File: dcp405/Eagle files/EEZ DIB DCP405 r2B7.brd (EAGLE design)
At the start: 180 x 95 mm, 311 parts, among them IC1 LTC3864EMSE#PBF, IC10 MC33272ADR2G, IC11 LTC2050HVCS8#PBF, IC12 74AUP1G74DC.125, IC13 MCP23S17-E/SS, IC14 REF5025AIDR, IC15 TC77-5.0MCTTR, IC16 DAC8552IDGKR, IC17 SN74LVC1G3157DCKR, IC18 ADS1120IPWR, IC19 LM293D, IC2 TPS54060DGQ, IC20 MAX9141ESA, IC3 SI8641BB-B-IS1, IC4 SN74LVC1G139DCUR, IC5 MC78L05, IC6 MC79L05, IC7 SI8641BB-B-IS1, IC8 M24C32-WMN6P, IC9 MC33272ADR2G, J1 4907, J2 FCR7350R, J3 FCR7350B, K1 G6K-2F-5DC, Q1 SUD19P06-60, Q10 PSMN0R9-25YLC, Q11 PSMN0R9-25YLC, Q12 BSS84P, Q13 BTA26-600, Q14 FMMT493TA, Q15 2N7002, Q16 2N7002, Q17 2N7002, Q18 MMBT5401, Q19 MMBT5551, Q2 MMBT5401, Q20 MMBT5551, Q21 2N7002, Q3 D45H11FP, Q4 D45H11FP, Q5 FQPF11P06 or FQPF27P06, Q6 BCP56-16.115, Q7 MMBT5401, Q8 NZT605, Q9 BSS205NH6327XTSA1, X1 39-30-1020, X2 77317-104-28LF, X3 1844249, X4 DS1024-2*10R0

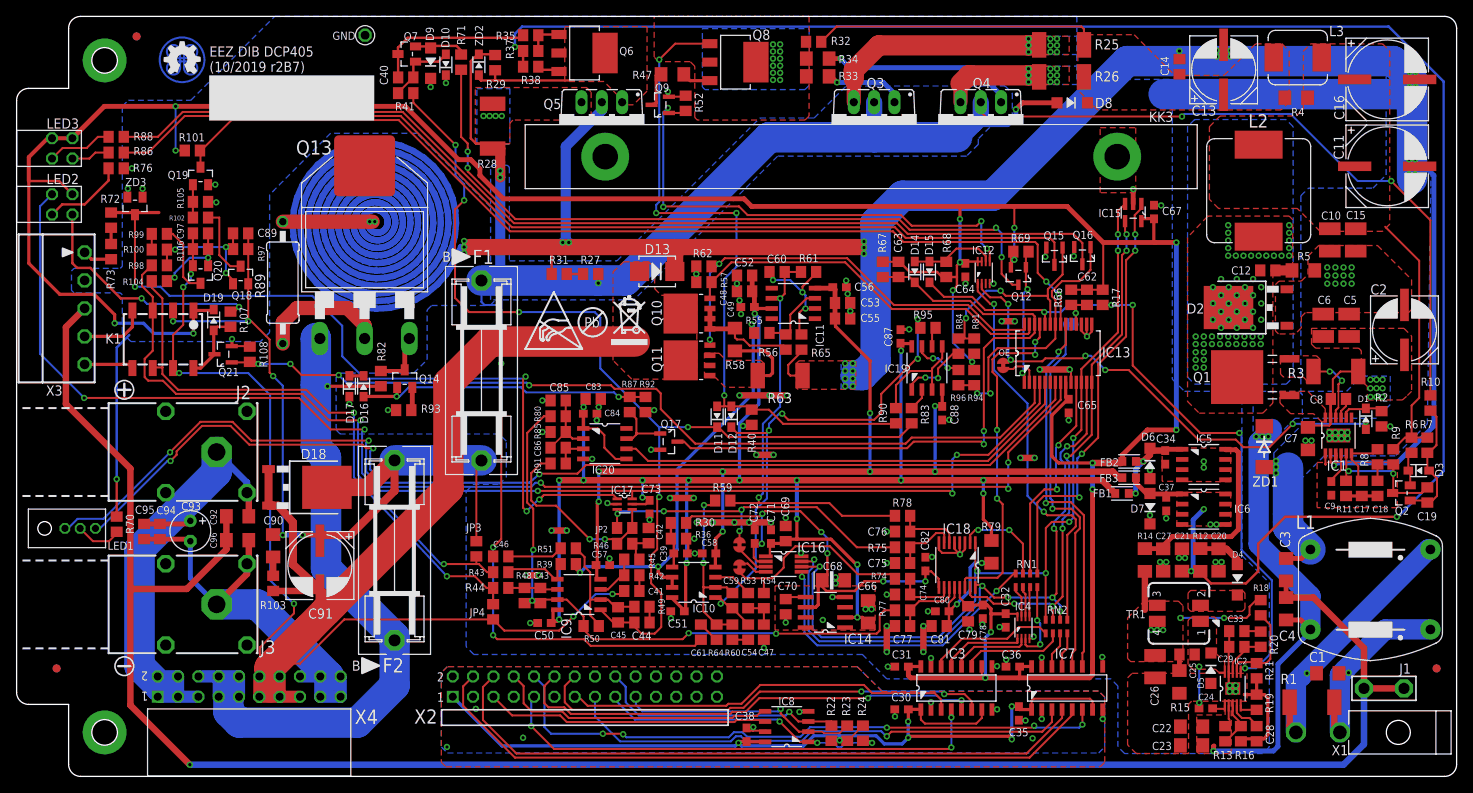
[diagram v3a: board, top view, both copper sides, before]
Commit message: DCP405 Q18 added to HW OVP
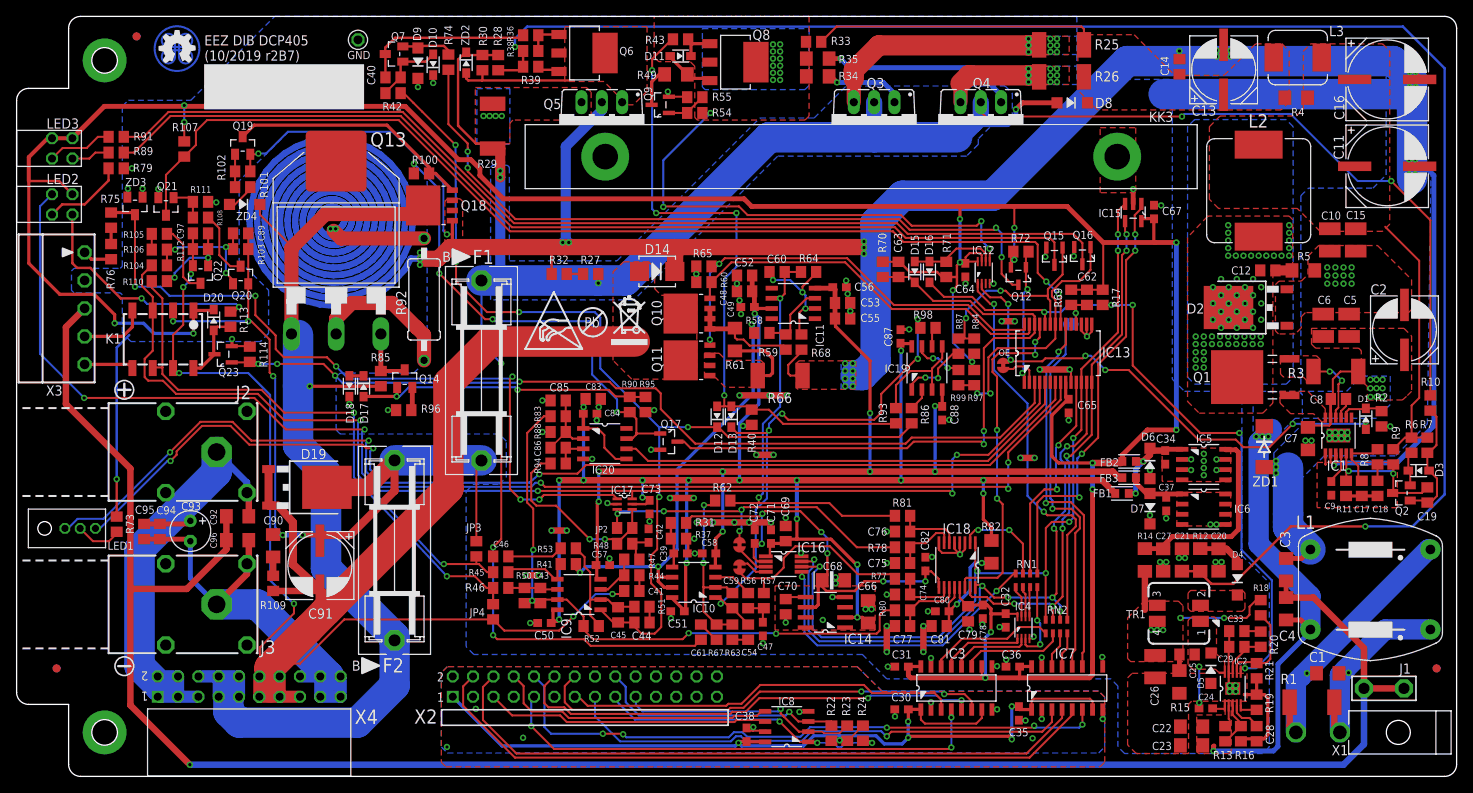
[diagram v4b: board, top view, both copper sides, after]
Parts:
- added D20: BAS316, EEZ_Lib1:SOD323-R
- added Q22: MMBT5551, transistor:SOT23-BEC
- added Q23: 2N7002, EEZ_Lib1:SOT103P240X110-3N
- added R109: 1R, rcl:R0805
- added R110: 750R, rcl:R0805
- added R111: 47K, rcl:R0805
- added R112: 330R, rcl:R0805
- added R113: 470R, rcl:R0805
- added R114: 100K, rcl:R0805
- added ZD4: MMSZ5230BT1G, EEZ_Lib1:SOD123
- C40: value 470p -> N.C.
- C41, C46: value 220p -> 100p
- C42, C47: value 470n -> 100n; device rcl:C0805 -> rcl:C0603
- C43, C60: value 33p -> N.C.
- C44: value 330p -> N.C.
- D13: value SK55 -> BAS316; device EEZ_Lib1:SMB -> EEZ_Lib1:SOD323-R
- D14: value BAS316 -> SK55; device EEZ_Lib1:SOD323-R -> EEZ_Lib1:SMB
- D18: value SK10100D1-DIO -> BAS316; device EEZ_Lib1:TO252-L -> EEZ_Lib1:SOD323-R
- D19: value BAS316 -> SK10100D1-DIO; device EEZ_Lib1:SOD323-R -> EEZ_Lib1:TO252-L
- IC9: value MC33272ADR2G -> TL072D
- Q18: value MMBT5401 -> PSMN013-60YL; device transistor:SOT23-BEC -> EEZ_Lib1:SOT669
- Q20: value MMBT5551 -> MMBT5401
- Q21: value 2N7002 -> MMBT5551; device EEZ_Lib1:SOT103P240X110-3N -> transistor:SOT23-BEC
- R100: value 2K2 -> 1K
- R101, R102: value 10K -> 22K
- R103: value 1R -> 330R
- R105: value 47K -> 1K
- R106, R80: value 330R -> 2K2
- R107: value 470R -> 10K
- R108, R52: value 100K -> 10K
- R28: value 2R2/2W -> 100K; device rcl:R2512 -> rcl:R0805
- R29: value 4K7 -> 2R2/2W; device rcl:R0805 -> rcl:R2512
- R30: value 10K -> 4K7
- R31, R67, R94: value 4K7 -> 10K
- R32: value 2K2 -> 4K7
- R33: value 10R -> 2K2; device rcl:R1206 -> rcl:R0805
- R35: value 5K6 -> 10R; device rcl:R0805 -> rcl:R1206
- R36: value 220R -> 4K7
- R37: value 1K -> 220R
- R38: value 220R -> 1K
- R39: value 7K5 0.1% -> 220R
- R41: value 22K -> 7K5 0.1%
- R42: value 4K7 -> 22K
- R43: value 124K 0.1% -> 1K
- R44: value 124K 0.1% -> 10K
- R45: value 10K -> 124K 0.1%
- R46: value 2K2 -> 124K 0.1%
- R47: value 15R -> 10K; device rcl:R1206 -> rcl:R0805
- R48: value 7K5 0.1% -> 2K2
- R49: value 2K2 -> 15R; device rcl:R0805 -> rcl:R1206
- R50: value 10K -> 7K5 0.1%
- R51: value 4K7 -> N.C.
- R53, R71: value 2K2 -> 10K
- R54: value 2K2 -> 220R
- R55: value 39K 0.1% -> 100K
- R56: value 820R 0.1% -> 2K2
- R57: value 47K -> 2K2
- R58: value 1R -> 39K 0.1%; device rcl:R1206 -> rcl:R0805
- R59, R68: value 10K -> 820R 0.1%
- R60: value 1K -> 47K
- R61: value 39K 0.1% -> 1R; device rcl:R0805 -> rcl:R1206
- R62: value 47K -> 10K
- R63: value 0R010 (low TCR) -> 1K; device EEZ_Lib1:R_2512-4WIRE -> rcl:R0805
- R64: value 10K -> 39K 0.1%
- R65: value 820R 0.1% -> 47K
- R66: value 1K -> 0R010 (low TCR); device rcl:R0805 -> EEZ_Lib1:R_2512-4WIRE
- R69: value 100K -> 1K
- R70: value 270R -> 4K7
- R72: value 470R -> 100K
- R73: value 470R -> 270R
- R75: value 2K2 -> 470R
- R79: value 10R -> 470R; device rcl:R1206 -> rcl:R0805
- R81: value 4K7 -> 2K2
- R82: value 470R -> 10R; device rcl:R0805 -> rcl:R1206
- R83, R91: value 10K -> 330R
- R85: value 10K -> 470R
- R86, R88: value 330R -> 10K
- R87, R99: value 1K -> 4K7
- R89: value AC01000001007JA100 -> 330R; device rcl:0411/15 -> rcl:R0805
- R90: value 10K -> 1K
- R92: value 100K -> AC01000001007JA100; device rcl:R0805 -> rcl:0411/15
- R93: value 6R2 -> 10K
- R95: value 10K -> 100K
- R96: value 4K7 -> 6R2
- R97: value 330R -> 4K7
- R98: value 750R -> 10K
- moved R79 119.5 mm to (12.4, 76.0), turned to 180 degrees
- moved R72 113.8 mm to (125.5, 65.6), turned to 0 degrees
- moved R75 107.1 mm to (11.8, 69.5), turned to 270 degrees
- moved R86 104.7 mm to (111.9, 45.1), turned to 90 degrees
- moved R99 101.5 mm to (117.7, 49.8), turned to 270 degrees
- moved R70 100.9 mm to (108.3, 63.4), turned to 270 degrees
- moved R98 96.4 mm to (113.9, 56.1)
- moved R97 93.1 mm to (119.7, 49.8), turned to 90 degrees
- moved R74 86.0 mm to (54.0, 89.3), turned to 270 degrees
- moved R82 79.3 mm to (121.9, 28.1)
- moved D16 72.2 mm to (114.1, 63.1), turned to 90 degrees
- moved R43 70.3 mm to (83.0, 92.1), turned to 0 degrees
- moved R96 69.5 mm to (48.4, 45.8), turned to 0 degrees
- moved R91 68.7 mm to (12.4, 79.9), turned to 180 degrees
- moved R42 67.2 mm to (47.1, 85.4)
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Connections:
- new net -9V: C21.1, R12.1, R28.1, R38.2, R39.2
- new net N$24: R101.2, ZD4.A
- new net N$28: Q19.B, R101.1, R102.2
- new net N$44: Q18.4, Q19.C, R100.1
- new net N$46: D11.C, Q8.1, R43.2
- new net N$53: Q9.1, R54.1, R55.2
- net !DP_DRIVE: now also R74.1; no longer R71.1
- net !IOEXP_RST: now also R69.2; no longer R66.2
- net !OVP_FAULT: now also D15.C, R70.2; no longer D14.C, R67.2
- net !SET_DP: now also R72.2; no longer R69.2
- net +5V: now also D20.C, R107.2, R70.1, R71.1, R72.1, R84.2, R97.2; no longer D19.C, R101.2, R66.1, R67.1, R68.1, R81.2, R94.2
- net +VREF: now also R31.1; no longer R30.1
- net -12V: no longer C21.1, R12.1, R37.2, R38.2
- net 50MA_S: now also R59.1, R61.1; no longer R56.1, R58.1
- net 5A_S: now also R66.2; no longer R63.2
- net AUX_IN: now also R75.1; no longer R72.1
- net CC_ACTIVE: now also R97.1, R99.2; no longer R94.1, R96.2
- net CC_LED: now also R91.2; no longer R88.2
- net CURR_50MA: now also R60.2; no longer R57.2
- net CURR_5A: now also R65.2; no longer R62.2
- net CV_ACTIVE: now also R84.1, R87.2; no longer R81.1, R84.2
- net CV_LED: now also R89.1; no longer R86.1
- net DARL_C: now also R35.1; no longer R32.1
- net DP_S: now also R29.1; no longer R28.1
- net D_CC: now also R91.1; no longer R88.1
- net D_CV: now also R89.2; no longer R86.2
- net GCOM: now also R41.1, R58.1; no longer R39.1, R55.1
- net GND: now also D18.C, Q21.E, Q23.2, R111.1, R114.1, R37.2, R55.1, R60.1, R65.1, R73.2, R79.1, R88.2, R95.1, R96.1; no longer D17.C, Q19.E, Q21.2, R105.1, R108.1, R36.2, R52.1, R57.1, R62.1, R70.2, R76.1, R85.2, R92.1, R93.1
- net ISENSE+: now also R58.2, R59.2; no longer R55.2, R56.2
- net ISENSE-: now also R64.1, R68.2; no longer R61.1, R65.2
- net I_MON: now also R62.1, R64.2, R81.1; no longer R59.1, R61.2, R78.1
- net I_SERVO: now also D13.C, R98.1; no longer D12.C, R95.1
- net I_SET: now also R57.1, R77.1; no longer R54.1, R74.1
- net LOOP_CTRL: now also D13.A, R43.1, R93.2; no longer D11.A, Q8.1, R90.2
- net N$10: now also R56.1, R57.2; no longer R53.1, R54.2
- net N$102: now also R31.2, R37.1; no longer R30.2, R36.1
- net N$105: now also R87.1; no longer R84.1
- net N$106: now also R99.1; no longer R96.1
- net N$107: now also Q20.B, R103.1, R104.2, R106.2; no longer Q18.B, R100.2, R97.1, R98.2
- net N$108: now also Q20.C, R108.2; no longer Q18.C, R102.2
- net N$109: now also Q22.C, R105.1; no longer Q20.C, R99.1
- net N$11: now also R61.2, R66.2S; no longer R58.2, R63.2S
- net N$110: now also Q22.B, R110.1, R112.2; no longer Q20.B, R104.1, R106.2
- net N$112: now also Q21.B, R108.1, R111.2; no longer Q19.B, R102.1, R105.2
- net N$113: now also R109.2; no longer R103.2
- net N$114: now also D20.A, Q23.3, R113.1; no longer D19.A, Q21.3, R107.1
- net N$12: now also R73.1; no longer R70.1
- net N$120: now also R113.2; no longer R107.2
- net N$121: now also R79.2; no longer R76.2
- net N$13: now also R100.2, R90.2; no longer R87.2
- net N$14: now also R51.2; no longer R49.2
- net N$15: now also R92.2; no longer R89.2
- net N$150: now also R41.2, R45.1; no longer R39.2, R43.1
- net N$153: now also R86.2; no longer R83.2
- net N$158: now also R46.1, R50.2; no longer R44.1, R48.2
- net N$161: now also R98.2; no longer R95.2
- net N$17: now also R75.2, R76.1; no longer R72.2, R73.1
- net N$170: now also R93.1; no longer R90.1
- net N$173: now also R105.2, R106.1; no longer R100.1, R99.2
- net N$18: now also R85.1; no longer R82.1
- net N$19: now also R96.2; no longer R93.2
- net N$20: now also D17.C, D18.A; no longer D16.C, D17.A
- net N$200: now also R66.1S, R68.1; no longer R63.1S, R65.1
- net N$21: now also D17.A, R90.1, R95.2; no longer D16.A, R87.1, R92.2
- net N$31: now also R94.2; no longer R91.2
- net N$32: now also R76.2; no longer R73.2
- net N$33: now also R83.2, R88.1; no longer R80.2, R85.1
- net N$35: now also R49.1; no longer R47.1
- net N$37: now also R63.1; no longer R60.1
- net N$39: now also R36.1, R38.1; no longer R35.1, R37.1
- net N$40: now also R35.2; no longer R34.2
- net N$42: now also R74.2; no longer R71.2
- net N$43: now also R34.2; no longer R33.2
- net N$45: now also R36.2; no longer R35.2
- net N$47: now also D11.A, R49.2; no longer R47.2
- net N$49: now also R32.2; no longer R31.2
- net N$55: now also R42.2; no longer R41.2
- net N$56: now also D16.A, R71.2; no longer D14.A, R68.2
- net N$70: now also R82.2; no longer R79.2
- net N$72: now also R77.2; no longer R74.2
- net N$73: now also R80.2; no longer R77.2
- net N$80: now also R78.2; no longer R75.2
- net N$81: now also R81.2; no longer R78.2
- net N$82: now also R56.2; no longer R53.2
- net N$83: now also R44.2, R47.2; no longer R42.2, R45.2
- net N$84: now also R51.1, R52.2, R53.2; no longer R49.1, R50.2, R51.2
- net N$88: now also R67.1; no longer R64.1
- net N$89: now also R62.2, R63.2, R67.2; no longer R59.2, R60.2, R64.2
- net N$90: now also R44.1; no longer R42.1
- net N$91: now also R53.1; no longer R51.1
- net N$98: now also R39.1; no longer R38.1
- net OUTF+: now also Q18.MB, R85.2, ZD4.C; no longer R82.2
- net POST_OE: now also R54.2; no longer Q9.1, R52.2
- net POST_OUT+: now also R29.2, R30.1; no longer R29.1
- net POST_OUT-: now also D14.A, D19.1, D19.2, Q22.E, R109.1, R112.1; no longer D13.A, D18.1, D18.2, Q20.E, R103.1, R106.1
- net POST_OUTF+: now also D19.3, Q20.E, R103.2; no longer D18.3, Q18.E, R97.2
- net PREG_OUT+: now also R33.2; no longer R32.2
- net PREG_OUT-: now also D14.C, Q18.1, Q18.2, Q18.3, Q19.E, R102.1, R32.1, R66.1, R92.1; no longer D13.C, R31.1, R63.1, R89.1
- net PWRGOOD: now also D16.C; no longer D15.C
- net Q6C: now also R30.2; no longer R29.2
- net RSENSE: now also Q23.1, R114.2; no longer Q21.1, R108.2
- net SENSE+: now also R104.1, R45.2; no longer R43.2, R98.1
- net SENSE-: now also R110.2, R46.2; no longer R104.2, R44.2
- net SENSE_ERR: now also Q21.C, R107.1; no longer Q19.C, R101.1
- net U_MON: now also R52.1, R83.1; no longer R48.1, R77.1
- net U_SERVO: now also D12.C, R42.1, R86.1; no longer D11.C, R41.1, R83.1
- net U_SET: now also R78.1; no longer R75.1
- net U_SET_OUT: now also R48.1, R94.1; no longer R46.1, R91.1
- net U_SET_OVP: now also R47.1, R48.2; no longer R45.1, R46.2
- net V+: now also R82.1; no longer R79.1
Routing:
- net -12V: track 222.5 -> 0.00 mm, vias 4 -> 0
- net -9V: track 0.00 -> 218.0 mm, vias 0 -> 2
- net N$13: track 8.24 -> 59.5 mm, vias 0 -> 4
- net PREG_OUT-: track 587.5 -> 631.7 mm, vias 23 -> 25
- net OUTF+: track 94.6 -> 134.0 mm
- net N$44: track 0.00 -> 30.6 mm
- net SENSE_ERR: track 125.9 -> 135.4 mm
- net AUX_IN: track 101.4 -> 96.1 mm, vias 4 -> 6
- net N$46: track 0.00 -> 5.17 mm
- net N$53: track 0.00 -> 5.04 mm
- net N$28: track 0.00 -> 4.11 mm
- net N$24: track 0.00 -> 3.64 mm
- net LOOP_CTRL: track 84.6 -> 81.2 mm
- net N$47: track 3.58 -> 6.45 mm
- net N$15: track 16.2 -> 18.5 mm
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
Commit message: DCP405 OE slow down
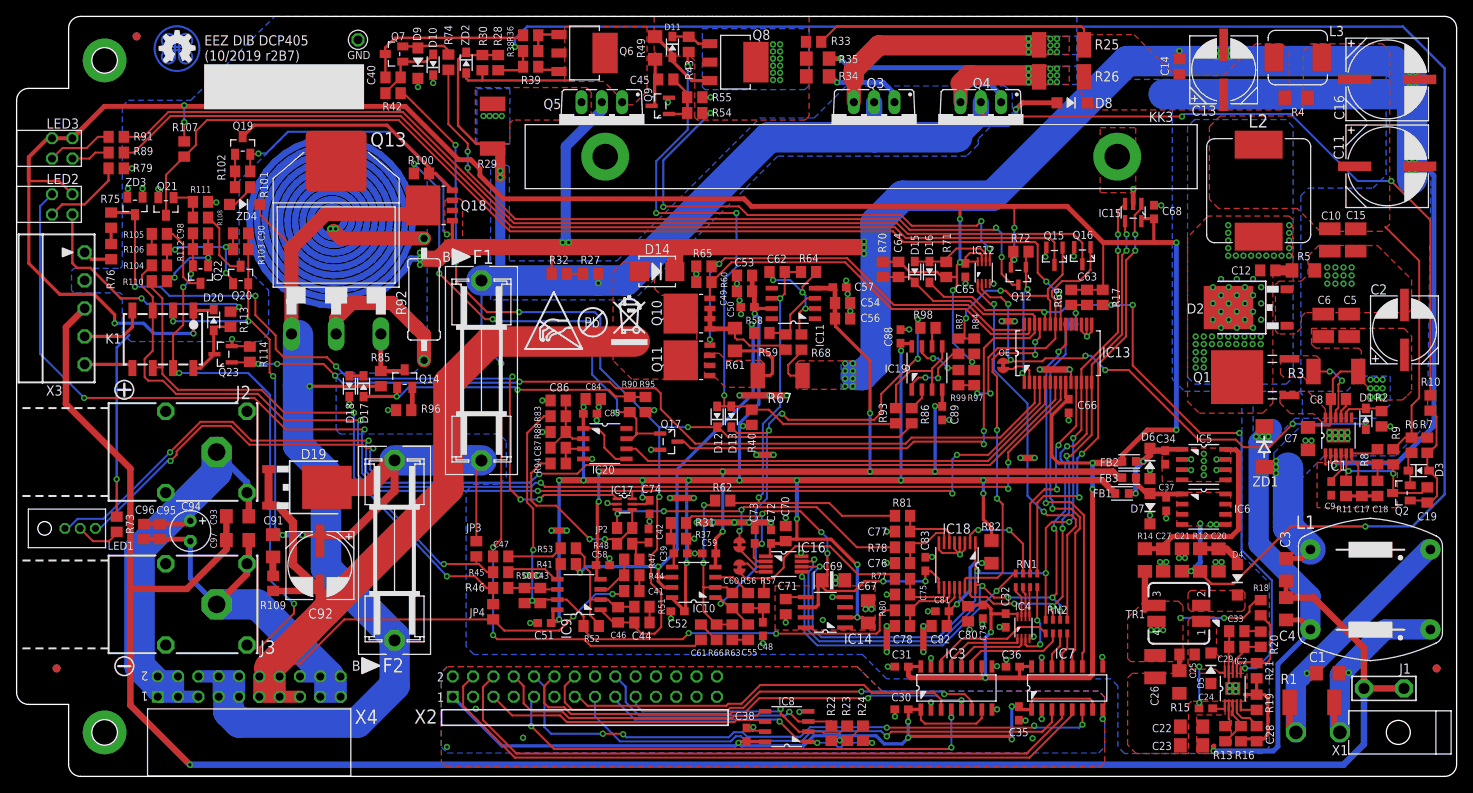
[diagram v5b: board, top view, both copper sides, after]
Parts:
- added C98: 10n, rcl:C0805
- C45: value 33p -> 1u
- C46: value 100p -> 33p
- C47: value 100n -> 100p; device rcl:C0603 -> rcl:C0805
- C48, C89: value 10n -> 100n; device rcl:C0805 -> rcl:C0603
- C49: value 100n -> 10n; device rcl:C0603 -> rcl:C0805
- C52, C79, C81: value 1u -> 100n; device rcl:C0805 -> rcl:C0603
- C53: value 10n -> 1u
- C54: value 6n8 -> 10n
- C55: value 1u -> 6n8
- C56, C71, C80, C82: value 100n -> 1u; device rcl:C0603 -> rcl:C0805
- C59: value 33p -> 100n; device rcl:C0805 -> rcl:C0603
- C60: value N.C. -> 33p
- C62: value 330p -> N.C.
- C63: value 1n -> 330p
- C64: value 100n -> 1n; device rcl:C0603 -> rcl:C0805
- C66: value 4u7 -> 100n; device rcl:C1206 -> rcl:C0603
- C67: value 100n -> 4u7; device rcl:C0603 -> rcl:C1206
- C68: value 4u7 tant. -> 100n; device EEZ_Lib1:EC1206 -> rcl:C0603
- C69: value 1u -> 4u7 tant.; device rcl:C0805 -> EEZ_Lib1:EC1206
- C74: value 4n7 -> 100n; device rcl:C0805 -> rcl:C0603
- C78: value 100n -> 4n7; device rcl:C0603 -> rcl:C0805
- C83: value N.C. -> 100n; device rcl:C0805 -> rcl:C0603
- C84: value 100n -> N.C.; device rcl:C0603 -> rcl:C0805
- C85: value 1n -> 100n; device rcl:C0805 -> rcl:C0603
- C86: value 33n -> 1n
- C87: value 100n -> 33n; device rcl:C0603 -> rcl:C0805
- C90: value 470n -> 10n; device rcl:C1206 -> rcl:C0805
- C91: value HHXC630A330MHA0G -> 470n; device EEZ_Lib1:CAPAE830X1050N -> rcl:C1206
- C92: value 10n/200V -> HHXC630A330MHA0G; device rcl:C1206 -> EEZ_Lib1:CAPAE830X1050N
- C93: value N.C. -> 10n/200V; device EEZ_Lib1:ECAP2/5 -> rcl:C1206
- C94: device rcl:C0805 -> EEZ_Lib1:ECAP2/5
- C96: value 10n/200V -> N.C.; device rcl:C1206 -> rcl:C0805
- C97: value 10n -> 10n/200V; device rcl:C0805 -> rcl:C1206
- KK1, KK2: value PCB-MB-01 -> PMB-1
- R44, R53: value 10K -> 16K
- R54: value 220R -> 4K7
- R55: value 100K -> N.C.
- R66: value 0R010 (low TCR) -> 10K; device EEZ_Lib1:R_2512-4WIRE -> rcl:R0805
- R67: value 10K -> 0R010 (low TCR); device rcl:R0805 -> EEZ_Lib1:R_2512-4WIRE
- moved C89 90.5 mm to (115.7, 45.4), turned to 90 degrees
- moved C45 67.2 mm to (81.2, 87.1), turned to 180 degrees
- moved C67 61.4 mm to (106.4, 20.6)
- moved C68 61.0 mm to (142.2, 70.5), turned to 90 degrees
- moved C50 47.0 mm to (91.4, 58.7), turned to 180 degrees
- moved C83 46.4 mm to (113.6, 26.5), turned to 270 degrees
- moved C57 45.6 mm to (102.9, 61.2), turned to 0 degrees
- moved C87 45.0 mm to (67.7, 41.1), turned to 0 degrees
- moved C54 42.8 mm to (103.3, 59.2), turned to 180 degrees
- moved C52 42.8 mm to (82.6, 20.6)
- moved C48 42.3 mm to (93.3, 18.4), turned to 270 degrees
- moved C60 41.5 mm to (89.5, 22.0), turned to 270 degrees
- moved C55 40.9 mm to (91.4, 18.0), turned to 90 degrees
- moved C90 39.3 mm to (28.0, 67.9), turned to 180 degrees
- moved C62 38.9 mm to (95.1, 63.1), turned to 0 degrees
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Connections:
- removed net -12V: IC6.2, IC6.3, IC6.6, IC6.7
- net !IOEXP_RST: now also C63.1; no longer C62.1
- net !OVP_FAULT: now also C64.1; no longer C63.1
- net +5V: now also C65.2, C66.1, C68.1, C80.2; no longer C62.2, C65.1, C67.1, C78.2
- net +VREF: now also C69.+, C73.2, C83.2; no longer C68.+, C72.2, C82.2
- net -9V: now also IC6.2, IC6.3, IC6.6, IC6.7
- net 5A_S: now also R67.2; no longer R66.2
- net GND: now also C48.2, C49.1, C50.2, C54.1, C56.1, C57.2, C59.1, C65.1, C68.2, C69.-, C71.2, C73.1, C74.2, C76.1, C77.2, C83.1, C84.2, C86.1, C89.1; no longer C47.2, C48.1, C49.2, C50.1, C55.1, C56.2, C57.1, C64.1, C65.2, C68.-, C69.2, C71.1, C73.2, C74.1, C76.2, C77.1, C83.2, C84.1, C87.1
- net ISENSE-: now also C62.1; no longer C60.1
- net I_MON: now also C62.2; no longer C60.2
- net I_SERVO: now also C55.2, C60.2; no longer C54.2, C59.2
- net N$10: now also C48.1; no longer C47.1
- net N$107: now also C90.2; no longer C89.2
- net N$11: now also R67.2S; no longer R66.2S
- net N$110: now also C98.1; no longer C97.1
- net N$113: now also C91.2; no longer C90.2
- net N$200: now also R67.1S; no longer R66.1S
- net N$31: now also C87.2; no longer C86.2
- net N$33: now also C86.2, C87.1; no longer C85.2, C86.1
- net N$35: now also C45.2
- net N$37: now also C55.1; no longer C54.1
- net N$53: now also C45.1
- net N$70: now also C82.2; no longer C80.2
- net N$71: now also C71.1; no longer C70.1
- net N$72: now also C75.2; no longer C74.2
- net N$73: now also C78.2; no longer C77.2
- net N$80: now also C76.2; no longer C75.2
- net N$81: now also C77.1; no longer C76.1
- net N$84: now also C46.1; no longer C45.1
- net N$88: now also R66.1; no longer R67.1
- net N$89: now also C60.1, R66.2; no longer C59.1, R67.2
- net N$91: now also C47.2; no longer C46.2
- net OUTC+: now also C93.1, C94.+, C96.1; no longer C92.1, C93.+, C94.1
- net OUTC-: now also C94.-, C97.2; no longer C93.-, C94.2
- net PE: now also C93.2, C97.1; no longer C92.2, C96.1
- net POST_OUT+: now also C47.1; no longer C46.1
- net POST_OUT-: now also C92.-, C98.2; no longer C91.-, C97.2
- net POST_OUTF+: now also C91.1, C92.+; no longer C89.1, C91.+
- net PREG_OUT-: now also R67.1; no longer R66.1
- net U_SERVO: now also C46.2; no longer C45.2
- net V+: now also C49.2, C50.1, C53.2, C67.1, C70.1, C72.2, C74.1, C84.1, C85.2, C88.2; no longer C48.2, C49.1, C50.2, C66.1, C69.1, C71.2, C73.1, C83.1, C84.2, C87.2
- net V-: now also C54.2, C56.2, C57.1, C59.2, C89.2; no longer C53.2, C55.2, C56.1, C57.2, C88.2
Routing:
- net -9V: track 218.0 -> 224.5 mm, vias 2 -> 4
- net N$47: track 6.45 -> 9.67 mm
- net N$53: track 5.04 -> 7.24 mm
- net N$35: track 4.88 -> 6.54 mm
- net LOOP_CTRL: track 81.2 -> 80.0 mm
- net OUTF+: track 134.0 -> 134.8 mm
- net GND: track 202.5 -> 202.2 mm, vias 121 -> 122
- added copper zone on layer 1, net -9V
- removed copper zone on layer 1, net -12V
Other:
- board text added: "0R"
- board text added: "Parts with red marked values are installed on DCP405 only Solder JP2, JP3, JP4 (0R 0805) and use wire jumper instead of F1 and F2 on DCP405B"

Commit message: DCP405 Eagle files updated
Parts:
- R28: value 100K -> N.C.
- X3: value 1844249 -> 691322110005
- moved C45 0.45 mm to (80.7, 87.2)
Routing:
- net LOOP_CTRL: track 80.0 -> 82.2 mm
- net POST_OE: track 61.7 -> 63.1 mm
- net -9V: track 224.5 -> 223.9 mm
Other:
- board text added: "EEZ DIB DCP405 (11/2019 r2B7)"
- board text added: "EEZ DIB DCP405 (11/2019 r2B7) DC power source 0-40V / 5A Project source code: github.com/eez-open"
- board text removed: "EEZ DIB DCP405 (10/2019 r2B7)"
- board text removed: "EEZ DIB DCP405 (10/2019 r2B7) DC power source 0-40V / 5A Project source code: github.com/eez-open"
